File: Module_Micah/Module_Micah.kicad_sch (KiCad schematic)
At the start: 2 parts

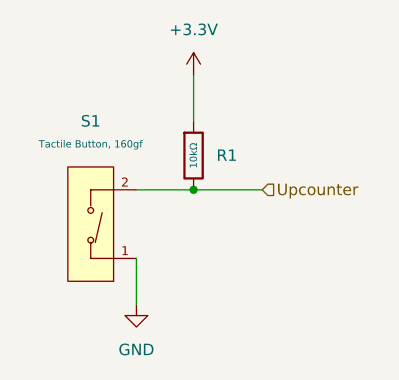
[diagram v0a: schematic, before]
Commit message: Imported Student Parts
Not using Project Instances yet.
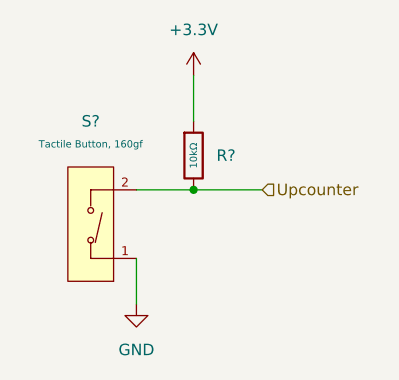
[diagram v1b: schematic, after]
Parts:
- renumbered R1 to R?, S1 to S?
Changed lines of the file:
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@@
 		(dnp no)
 		(fields_autoplaced yes)
-		(property "Reference" "S1"
+		(property "Reference" "S?"
 			(at 146.05 106.68 0)
 			(effects
@@
 			(project ""
 				(path "/c12dc015-e6cb-468c-8de4-269c3106de0e/81e179b3-10f3-4413-89ac-746efb52a96a"
-					(reference "S1")
+					(reference "S?")
 					(unit 1)
 				)
@@
 		(dnp no)
 		(fields_autoplaced yes)
-		(property "Reference" "#PWR02"
+		(property "Reference" "#PWR?"
 			(at 157.48 105.41 0)
 			(effects
@@
 			(project ""
 				(path "/c12dc015-e6cb-468c-8de4-269c3106de0e/81e179b3-10f3-4413-89ac-746efb52a96a"
-					(reference "#PWR02")
+					(reference "#PWR?")
 					(unit 1)
 				)
@@
 		(dnp no)
 		(fields_autoplaced yes)
-		(property "Reference" "#PWR01"
+		(property "Reference" "#PWR?"
 			(at 151.13 133.35 0)
 			(effects
@@
 			(project ""
 				(path "/c12dc015-e6cb-468c-8de4-269c3106de0e/81e179b3-10f3-4413-89ac-746efb52a96a"
-					(reference "#PWR01")
+					(reference "#PWR?")
 					(unit 1)
 				)
@@
 		(on_board yes)
 		(dnp no)
-		(property "Reference" "R1"
+		(property "Reference" "R?"
 			(at 160.02 110.4899 0)
 			(effects
@@
 			(project ""
 				(path "/c12dc015-e6cb-468c-8de4-269c3106de0e/81e179b3-10f3-4413-89ac-746efb52a96a"
-					(reference "R1")
+					(reference "R?")
 					(unit 1)
 				)

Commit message: Going to school.
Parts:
- gave numbers to parts that had none: 2
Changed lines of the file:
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@@
 		(dnp no)
 		(fields_autoplaced yes)
-		(property "Reference" "S?"
+		(property "Reference" "S2"
 			(at 146.05 106.68 0)
 			(effects
@@
 			(project ""
 				(path "/c12dc015-e6cb-468c-8de4-269c3106de0e/81e179b3-10f3-4413-89ac-746efb52a96a"
-					(reference "S?")
+					(reference "S2")
 					(unit 1)
 				)
@@
 		(dnp no)
 		(fields_autoplaced yes)
-		(property "Reference" "#PWR?"
+		(property "Reference" "#PWR0126"
 			(at 157.48 105.41 0)
 			(effects
@@
 			(project ""
 				(path "/c12dc015-e6cb-468c-8de4-269c3106de0e/81e179b3-10f3-4413-89ac-746efb52a96a"
-					(reference "#PWR?")
+					(reference "#PWR0126")
 					(unit 1)
 				)
@@
 		(dnp no)
 		(fields_autoplaced yes)
-		(property "Reference" "#PWR?"
+		(property "Reference" "#PWR0125"
 			(at 151.13 133.35 0)
 			(effects
@@
 			(project ""
 				(path "/c12dc015-e6cb-468c-8de4-269c3106de0e/81e179b3-10f3-4413-89ac-746efb52a96a"
-					(reference "#PWR?")
+					(reference "#PWR0125")
 					(unit 1)
 				)
@@
 		(on_board yes)
 		(dnp no)
-		(property "Reference" "R?"
+		(property "Reference" "R70"
 			(at 160.02 110.4899 0)
 			(effects
@@
 			(project ""
 				(path "/c12dc015-e6cb-468c-8de4-269c3106de0e/81e179b3-10f3-4413-89ac-746efb52a96a"
-					(reference "R?")
+					(reference "R70")
 					(unit 1)
 				)

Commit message: No Errors No Warnings
Some were excluded.
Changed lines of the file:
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@@
 	)
 	(hierarchical_label "Upcounter"
-		(shape input)
+		(shape output)
 		(at 165.1 114.3 0)
 		(effects

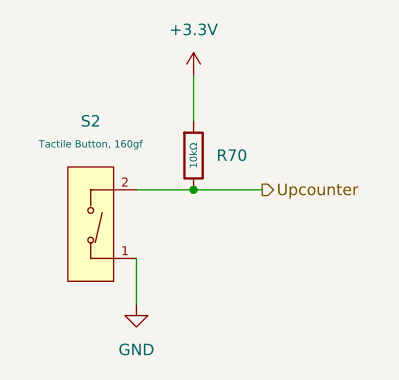
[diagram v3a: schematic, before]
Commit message: Replaced Jaron's LEDs
They were only for Standard Boards.
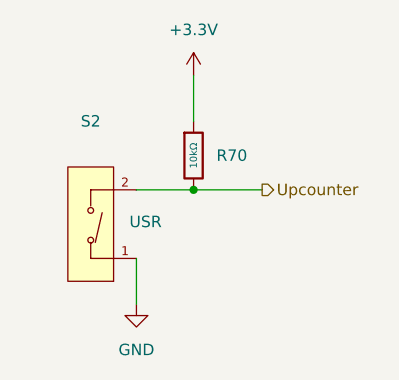
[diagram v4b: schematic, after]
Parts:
- S2: Label (none) -> USR
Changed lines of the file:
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@@
 		(on_board yes)
 		(dnp no)
-		(fields_autoplaced yes)
 		(property "Reference" "S2"
 			(at 146.05 106.68 0)
@@
 					(size 0.8 0.8)
 				)
+				(hide yes)
 			)
 		)
@@
 			)
 		)
+		(property "Label" "USR"
+			(at 152.146 117.856 0)
+			(effects
+				(font
+					(size 1.27 1.27)
+				)
+			)
+		)

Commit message: Placed the second ADC
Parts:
- R70: Manufacturer UNI-ROYAL(Uniroyal Elec) -> (none)
- S2: Manufacturer XUNPU -> (none)
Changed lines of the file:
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@@
-			)
-		)
-		(property "Manufacturer" "XUNPU"
-			(at 146.05 119.38 0)
-			(hide yes)
-			(show_name no)
-			(do_not_autoplace no)
-			(effects
-				(font
-					(size 1.27 1.27)
-				)
 			)
 		)
@@
 			(at 157.48 110.49 0)
 			(hide yes)
-			(show_name no)
-			(do_not_autoplace no)
-			(effects
-				(font
-					(size 1.27 1.27)
-				)
-			)
-		)
-		(property "Manufacturer" "UNI-ROYAL(Uniroyal Elec)"
-			(at 157.48 110.49 0)
-			(hide yes)
